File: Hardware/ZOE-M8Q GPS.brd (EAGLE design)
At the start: 25.4 x 25.4 mm, 60 parts, among them J4 U.FL, U1 UBLOX_ZOE_M8-0-10, Y1 32.768kHz

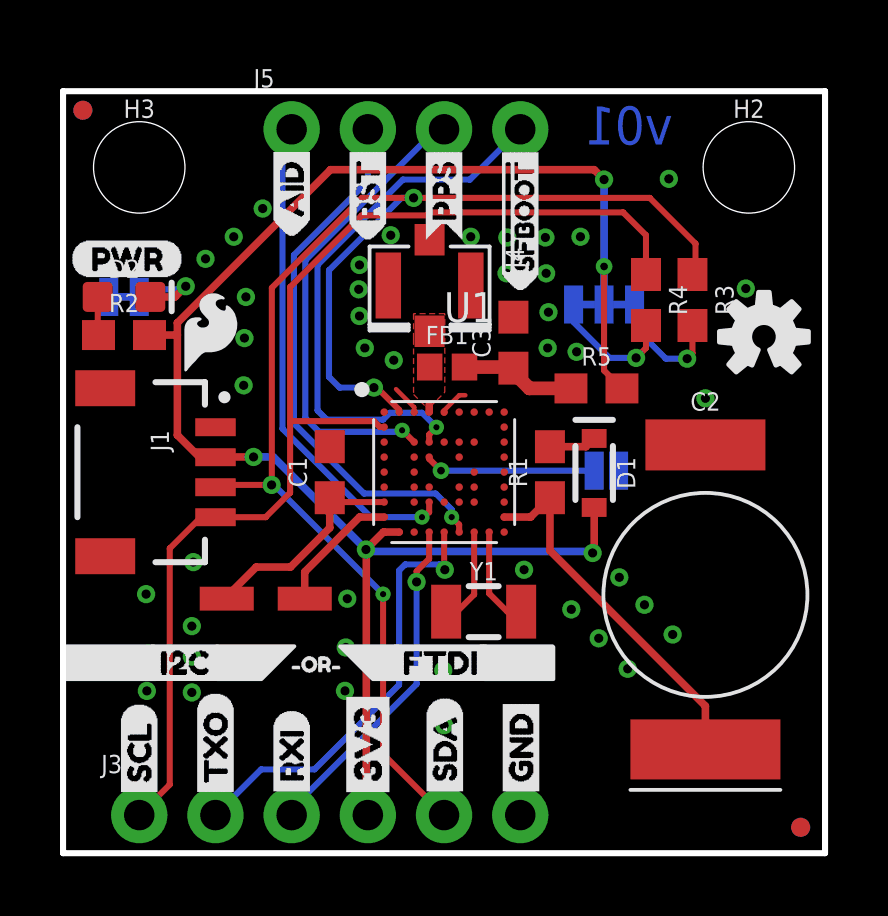
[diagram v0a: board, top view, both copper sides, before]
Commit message: Adds new reflowable battery, updates battery, inductor, and IC with versions in the SparkFun Eagle Library
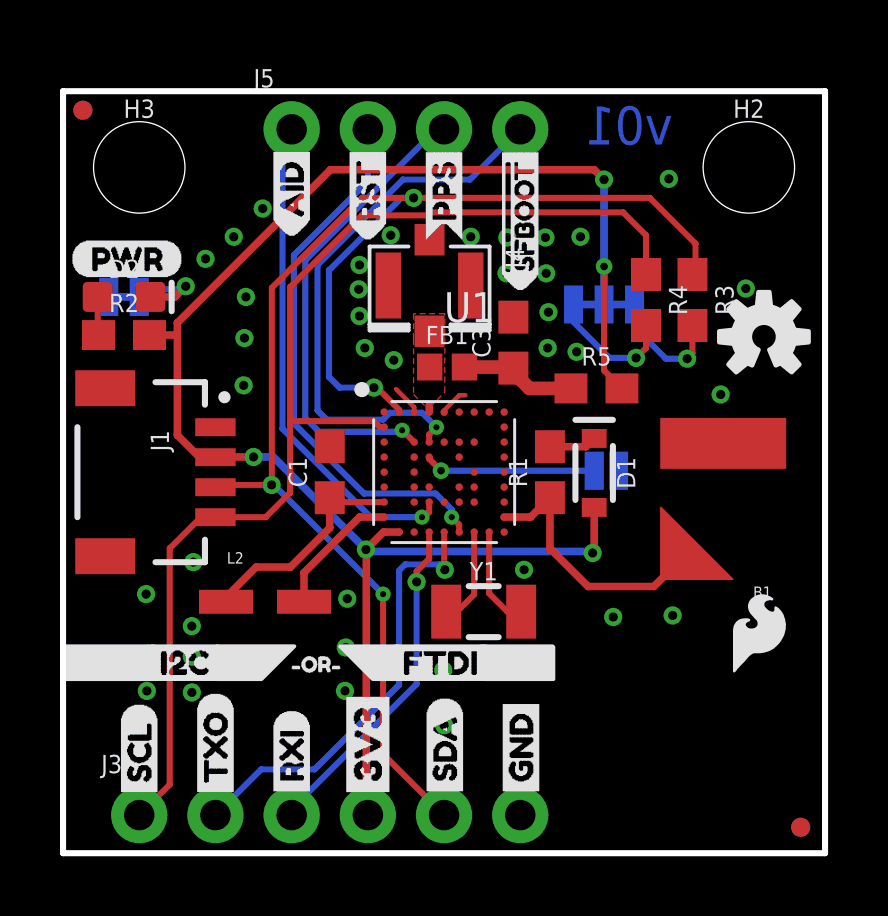
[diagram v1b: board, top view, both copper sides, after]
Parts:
- removed C2: .22F-SUPERCAP, SparkFun-Capacitors:DSK-RADIAL-4.8MM
- removed L1: 2.2UH_SHIELDED_INDUCTOR, temp:0806_NDUC
- added B1: ML414H_IV01E_BATTERY, SparkFun-Batteries:ML414H_IV01E
- added L2: 2.2UH_SHIELDED_INDUCTOR, SparkFun-Coils:UNIQUE_0806_NDUC
- U1: device temp:UBLOX_ZOE_M8-0-10 -> SparkFun-GPS:UBLOX_ZOE_M8-0-10
- moved LOGO3 20.9 mm to (23.2, 7.35)
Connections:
- net GND: now also B1.-; no longer C2.-
- net N$6: now also L2.1; no longer L1.P$1
- net N$7: now also L2.2; no longer L1.P$2
- net V_BATT: now also B1.+; no longer C2.+
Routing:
- net V_BATT: track 12.3 -> 8.81 mm
- net GND: vias 43 -> 39
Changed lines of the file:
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@@
 <layer number="37" name="tTest" color="7" fill="1" visible="no" active="yes"/>
 <layer number="38" name="bTest" color="7" fill="1" visible="no" active="yes"/>
-<layer number="39" name="tKeepout" color="4" fill="11" visible="yes" active="yes"/>
+<layer number="39" name="tKeepout" color="4" fill="11" visible="no" active="yes"/>
 <layer number="40" name="bKeepout" color="1" fill="11" visible="no" active="yes"/>
 <layer number="41" name="tRestrict" color="4" fill="10" visible="no" active="yes"/>
@@
 <layer number="45" name="Holes" color="7" fill="1" visible="yes" active="yes"/>
 <layer number="46" name="Milling" color="3" fill="1" visible="no" active="yes"/>
-<layer number="47" name="Measures" color="7" fill="1" visible="yes" active="yes"/>
+<layer number="47" name="Measures" color="7" fill="1" visible="no" active="yes"/>
 <layer number="48" name="Document" color="7" fill="1" visible="no" active="yes"/>
 <layer number="49" name="Reference" color="13" fill="1" visible="yes" active="yes"/>
@@
 <attribute name="REV" value="" x="-7.62" y="-12.7" size="1.778" layer="27" font="vector" ratio="15" display="off"/>
 </element>
-<element name="U1" library="temp" package="UBLOX_ZOE_M8-0-10" value="UBLOX_ZOE_M8-0-10" x="12.7" y="12.7" smashed="yes">
+<element name="U1" library="SparkFun-GPS" package="UBLOX_ZOE_M8-0-10" value="UBLOX_ZOE_M8-0-10" x="12.7" y="12.7" smashed="yes">
 <attribute name="NAME" x="12.7" y="17.7" size="1" layer="25"/>
 <attribute name="PROD_ID" value="IC-14251" x="12.7" y="12.7" size="1.778" layer="27" font="vector" ratio="15" display="off"/>
@@
 <element name="LOGO2" library="SparkFun-Aesthetics" package="OSHW-LOGO-S" value="OSHW-LOGOS" x="23.362921875" y="17.213578125" smashed="yes"/>
 <element name="U$16" library="ZOE-M8Q" package="ZOE#M8Q0" value="" x="12.7508" y="12.6238" smashed="yes" rot="MR0"/>
-<element name="LOGO3" library="SparkFun-Aesthetics" package="SFE_LOGO_FLAME_.1" value="SFE_LOGO_FLAME.1_INCH" x="4.9047375" y="17.386303125" smashed="yes"/>
+<element name="LOGO3" library="SparkFun-Aesthetics" package="SFE_LOGO_FLAME_.1" value="SFE_LOGO_FLAME.1_INCH" x="23.1927375" y="7.353303125" smashed="yes"/>
 <element name="U$17" library="SPI_JUMPER" package="SPI0" value="" x="19.558" y="10.922" smashed="yes" rot="MR0"/>
 <element name="U$18" library="I2C_PU" package="I2C_PU0" value="" x="20.447" y="16.51" smashed="yes" rot="MR0"/>
@@
 <element name="U$29" library="FTDI_SMALL" package="FTDI0" value="" x="10.6426" y="6.35" smashed="yes"/>
 <element name="U$30" library="OR" package="#OR#0" value="" x="7.1628" y="6.2992" smashed="yes"/>
-<element name="C2" library="SparkFun-Capacitors" package="DSK-RADIAL-4.8MM" value=".22F-SUPERCAP" x="21.4122" y="8.6106" smashed="yes" rot="R180">
-<attribute name="NAME" x="21.4122" y="15.0556" size="0.6096" layer="25" font="vector" ratio="20" rot="R180" align="center"/>
-<attribute name="PROD_ID" value="CAP-13907" x="21.4122" y="8.6106" size="1.27" layer="27" font="vector" ratio="15" rot="R180" display="off"/>
-<attribute name="VALUE" x="21.4122" y="1.5306" size="0.6096" layer="27" font="vector" ratio="20" rot="R180" align="center"/>
-</element>
 <element name="FB1" library="SparkFun-Coils" package="0402" value="FERRITE_BEAD-120_OHM-0402" x="12.8016" y="16.2052" smashed="yes">
 <attribute name="MFG_PART" value="BLM15HB121SN1D" x="12.8016" y="16.2052" size="1.27" layer="27" font="vector" ratio="15" display="off"/>
@@
 <attribute name="VALUE" x="15.7734" y="17.018" size="0.6096" layer="27" font="vector" ratio="20" rot="R90" align="top-center"/>
 </element>
-<element name="L1" library="temp" package="0806_NDUC" value="2.2UH_SHIELDED_INDUCTOR" x="6.7564" y="8.4836" smashed="yes"/>
+<element name="B1" library="SparkFun-Batteries" package="ML414H_IV01E" value="ML414H_IV01E_BATTERY" x="22.606" y="11.811" smashed="yes" rot="R180">
+<attribute name="NAME" x="23.622" y="8.89" size="0.381" layer="25" rot="R180"/>
+<attribute name="PROD_ID" value="BATT-14267" x="22.606" y="11.811" size="1.778" layer="27" font="vector" ratio="15" rot="R180" display="off"/>
+<attribute name="VALUE" x="23.622" y="15.113" size="0.381" layer="27" rot="R180"/>
+</element>
+<element name="L2" library="SparkFun-Coils" package="UNIQUE_0806_NDUC" value="2.2UH_SHIELDED_INDUCTOR" x="6.731" y="8.382" smashed="yes">
+<attribute name="NAME" x="5.461" y="9.652" size="0.381" layer="25"/>
+<attribute name="PROD_ID" value="NDUC-14257" x="6.731" y="8.382" size="1.778" layer="27" font="vector" ratio="15" display="off"/>
+<attribute name="VALUE" x="5.461" y="6.858" size="0.381" layer="27"/>
+</element>
 </elements>
 <signals>
@@
 </polygon>
 <contactref element="JP1" pad="2"/>
-<via x="21.4122" y="15.1638" extent="1-16" drill="0.3048"/>
+<via x="21.9202" y="15.2908" extent="1-16" drill="0.3048"/>
 <via x="20.193" y="22.479" extent="1-16" drill="0.3048"/>
-<via x="16.9418" y="8.128" extent="1-16" drill="0.3048"/>
+<via x="18.3388" y="7.874" extent="1-16" drill="0.3048"/>
 <via x="4.2926" y="5.3594" extent="1-16" drill="0.3048"/>
 <via x="12.6746" y="6.096" extent="1-16" drill="0.3048"/>
@@
 <via x="9.4742" y="8.4836" extent="1-16" drill="0.3048"/>
 <via x="4.3434" y="9.7028" extent="1-16" drill="0.3048"/>
-<contactref element="C2" pad="-"/>
 <contactref element="C3" pad="2"/>
 <contactref element="J4" pad="1"/>
@@
 <via x="6.6548" y="21.4884" extent="1-16" drill="0.3048"/>
 <via x="4.7498" y="19.812" extent="1-16" drill="0.3048"/>
-<via x="18.542" y="9.1948" extent="1-16" drill="0.3048"/>
-<via x="19.3802" y="8.2804" extent="1-16" drill="0.3048"/>
-<via x="20.32" y="7.2898" extent="1-16" drill="0.3048"/>
-<via x="17.8562" y="7.1628" extent="1-16" drill="0.3048"/>
-<via x="18.8214" y="6.1468" extent="1-16" drill="0.3048"/>
+<via x="20.32" y="7.9248" extent="1-16" drill="0.3048"/>
 <via x="2.8194" y="6.6548" extent="1-16" drill="0.3048"/>
 <via x="2.794" y="5.4102" extent="1-16" drill="0.3048"/>
@@
 <wire x1="11.704" y1="14.8644" x2="11.0998" y2="15.4686" width="0.1524" layer="1"/>
 <wire x1="12.704" y1="14.704" x2="12.704" y2="14.6786" width="0.2032" layer="1"/>
+<contactref element="B1" pad="-"/>
 </signal>
 <signal name="3.3V">
@@
 <signal name="N$7">
 <contactref element="U1" pad="26"/>
-<wire x1="10.704" y1="11.204" x2="9.8832" y2="11.204" width="0.254" layer="1"/>
-<wire x1="9.8832" y1="11.204" x2="8.0564" y2="9.3772" width="0.254" layer="1"/>
-<contactref element="L1" pad="P$2"/>
-<wire x1="8.0564" y1="9.3772" x2="8.0564" y2="8.4836" width="0.254" layer="1"/>
+<wire x1="9.8832" y1="11.204" x2="10.704" y2="11.204" width="0.254" layer="1"/>
+<contactref element="L2" pad="2"/>
+<wire x1="8.031" y1="8.382" x2="8.031" y2="9.3518" width="0.254" layer="1"/>
+<wire x1="8.031" y1="9.3518" x2="9.8832" y2="11.204" width="0.254" layer="1"/>
 </signal>
 <signal name="N$6">
@@
 <wire x1="8.89" y1="10.8458" x2="7.5819" y2="9.5377" width="0.254" layer="1"/>
 <wire x1="7.5819" y1="9.5377" x2="6.4389" y2="9.5377" width="0.254" layer="1"/>
-<contactref element="L1" pad="P$1"/>
-<wire x1="6.4389" y1="9.5377" x2="5.4564" y2="8.5552" width="0.254" layer="1"/>
-<wire x1="5.4564" y1="8.5552" x2="5.4564" y2="8.4836" width="0.254" layer="1"/>
+<contactref element="L2" pad="1"/>
+<wire x1="6.4389" y1="9.5377" x2="5.431" y2="8.5298" width="0.254" layer="1"/>
+<wire x1="5.431" y1="8.5298" x2="5.431" y2="8.382" width="0.254" layer="1"/>
 </signal>
 <signal name="V_BATT">
@@
 <contactref element="R1" pad="1"/>
 <wire x1="14.704" y1="11.204" x2="15.5846" y2="11.204" width="0.254" layer="1"/>
-<wire x1="16.2306" y1="11.85" x2="16.2306" y2="10.086328125" width="0.254" layer="1"/>
+<wire x1="16.2306" y1="11.85" x2="16.2306" y2="10.16" width="0.254" layer="1"/>
+<wire x1="16.2306" y1="10.16" x2="16.2306" y2="10.086328125" width="0.254" layer="1"/>
 <wire x1="15.5846" y1="11.204" x2="16.2306" y2="11.85" width="0.254" layer="1"/>
-<contactref element="C2" pad="+"/>
-<wire x1="16.2306" y1="10.086328125" x2="21.4122" y2="4.904728125" width="0.254" layer="1"/>
-<wire x1="21.4122" y1="4.904728125" x2="21.4122" y2="3.4606" width="0.254" layer="1"/>
+<wire x1="17.5006" y1="8.89" x2="16.2306" y2="10.16" width="0.254" layer="1"/>
+<contactref element="B1" pad="+"/>
+<wire x1="20.584" y1="9.779" x2="19.695" y2="8.89" width="0.254" layer="1"/>
+<wire x1="19.695" y1="8.89" x2="17.5006" y2="8.89" width="0.254" layer="1"/>
 </signal>
 <signal name="TXO/MISO">

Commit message: Adds more ground vias, ZOE silk to topside, adjusts safteboot trace away from RF in, adds .1uF capactior
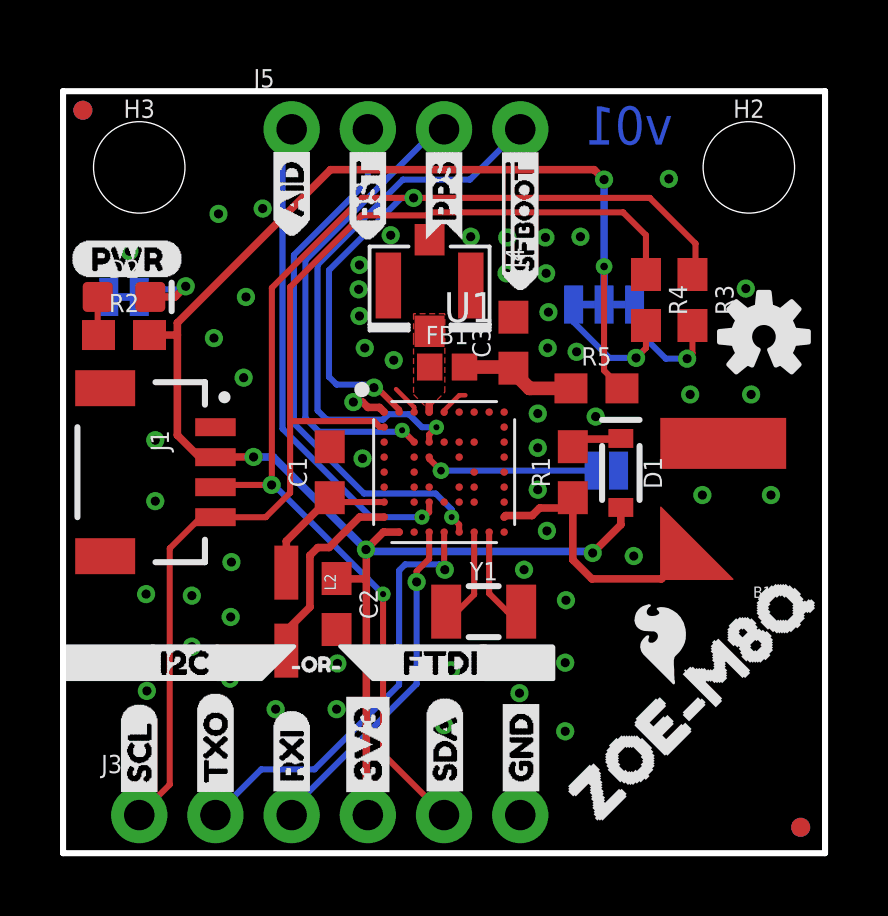
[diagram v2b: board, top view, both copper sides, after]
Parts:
- added C2: 0.1uF, SparkFun-Capacitors:0603
- added U$20: (no value), ZOE-M8Q:ZOE#M8Q0
- moved LOGO3 3.17 mm to (20.0, 7.16), turned to 45 degrees
- moved D1 0.89 mm to (18.6, 12.7)
- moved L2 0.78 mm to (7.44, 8.05), turned to 270 degrees
- moved R1 0.76 mm to (17.0, 12.7)
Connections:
- net 3.3V: now also C2.1
- net GND: now also C2.2
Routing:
- net N$6: track 7.48 -> 5.14 mm
- net N$7: track 4.41 -> 6.50 mm
- net 3.3V: track 56.9 -> 58.2 mm
- net GND: track 2.01 -> 3.18 mm, vias 39 -> 54
